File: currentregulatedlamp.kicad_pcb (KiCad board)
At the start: 2 copper layers, 9 parts, among them J1 Conn_01x12, J2 Conn_01x16, U1 TPS54308DDC

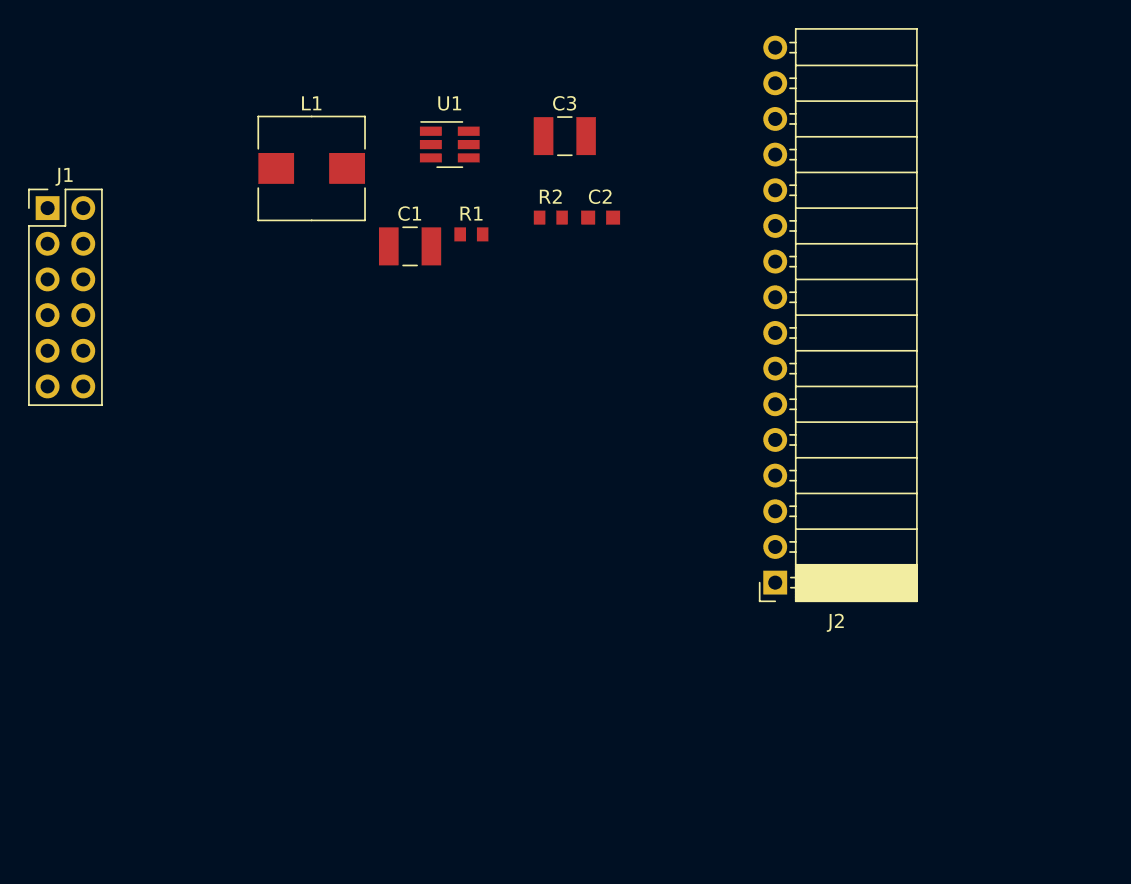
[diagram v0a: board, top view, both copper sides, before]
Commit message: include libraries
added project specific libraries that allow porting the design
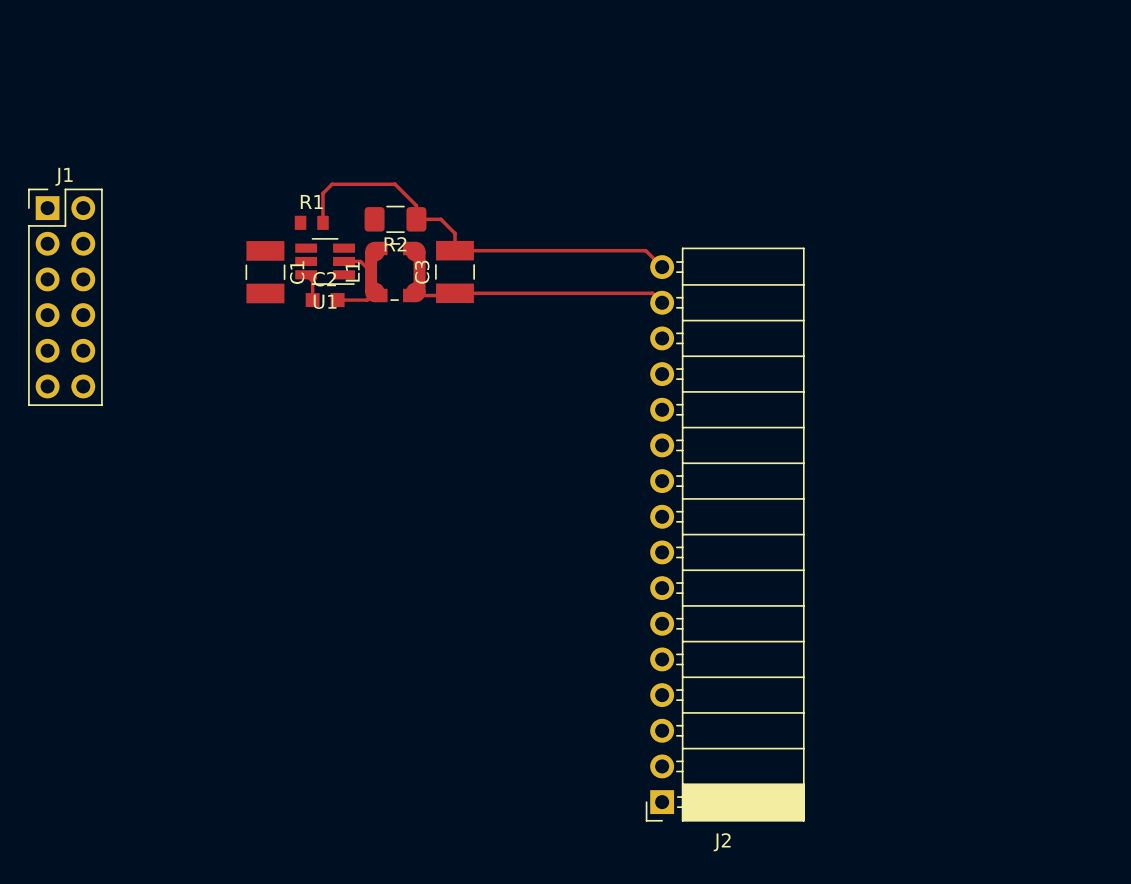
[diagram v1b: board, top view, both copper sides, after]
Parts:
- C2: value C -> 100n/50V
- L1: footprint Inductor_SMD:L_Wuerth_HCM-7070 -> Inductor_SMD:L_Wuerth_WE-TPC-3816
- R2: footprint Resistor_SMD:R_0603_1608Metric -> Resistor_SMD:R_1206_3216Metric_Pad1.42x1.75mm_HandSolder
- moved C2 20.5 mm to (50.8, 51.0)
- moved J2 17.6 mm to (74.8, 86.8)
- moved C3 12.4 mm to (60.0, 49.0), turned to 90 degrees
- moved U1 12.2 mm to (50.8, 48.2), turned to 180 degrees
- moved R1 11.4 mm to (49.8, 45.5)
- moved R2 11.1 mm to (55.8, 45.2), turned to 180 degrees
- moved C1 10.5 mm to (46.5, 49.0), turned to 270 degrees
- moved L1 9.48 mm to (55.8, 49.0), turned to 90 degrees
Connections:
- J2 pad 1: /TPS54200/LED+ -> Net-(J2-Pad1)
- J2 pad 15: Net-(J2-Pad15) -> /TPS54200/LED+
- J2 pad 16: Net-(J2-Pad16) -> /TPS54200/LED-
- J2 pad 2: /TPS54200/LED- -> Net-(J2-Pad2)
- L1 pad 1: /TPS54200/BOOT -> /TPS54200/SW
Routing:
- net /TPS54200/LED-: track 0.00 -> 30.3 mm
- net /TPS54200/LED+: track 0.00 -> 20.4 mm
- net /TPS54200/SW: track 0.00 -> 5.13 mm
- net /TPS54200/BOOT: track 0.00 -> 1.99 mm

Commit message: Schematic replication
decided on path for replicating current regulator
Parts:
- added C1.2: C, Capacitor_SMD:C_1210_3225Metric_Pad1.39x2.70mm_HandSolder, F.Cu at (65.0, 53.5)
- added C2.2: 100n/50V, Capacitor_SMD:C_0603_1608Metric_Pad0.99x1.00mm_HandSolder, F.Cu at (70.2, 56.0)
- added C3.2: C, Capacitor_SMD:C_1210_3225Metric_Pad1.39x2.70mm_HandSolder, F.Cu at (79.5, 54.0)
- added L1.2: L, Inductor_SMD:L_Wuerth_WE-TPC-3816, F.Cu at (75.2, 54.0)
- added R1.2: R, Resistor_SMD:R_0603_1608Metric, F.Cu at (69.3, 50.5)
- added R2.2: R, Resistor_SMD:R_1206_3216Metric_Pad1.42x1.75mm_HandSolder, F.Cu at (75.3, 50.2)
- added U1.2: TPS54308DDC, Package_TO_SOT_SMD:SOT-23-6_Handsoldering, F.Cu at (70.2, 53.2)
- moved J2 21.3 mm to (96.0, 85.7)
- moved J1 3.14 mm to (31.8, 47.5)
- moved C1.1 1.28 mm to (45.2, 48.8)
- renumbered C1 to C1.1, C2 to C2.1, C3 to C3.1, L1 to L1.1, R1 to R1.1, R2 to R2.1, U1 to U1.1
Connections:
- J1 pad 6: Net-(J1-Pad6) -> /LED_2/DIM
- J2 pad 15: /TPS54200/LED+ -> Net-(J2-Pad15)
- J2 pad 16: /TPS54200/LED- -> Net-(J2-Pad16)
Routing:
- net /LED-: track 0.00 -> 50.8 mm
- net /LED+: track 0.00 -> 43.5 mm
- net /TPS54200/LED-: track 30.3 -> 0.00 mm
- net /LED_2/LED-: track 0.00 -> 27.8 mm
- net /TPS54200/LED+: track 20.4 -> 0.00 mm
- net /LED_2/LED+: track 0.00 -> 19.5 mm
- net /LED_2/SW: track 0.00 -> 5.13 mm
- net /LED_2/BOOT: track 0.00 -> 1.99 mm
- net /LED_2/FB: track 0.00 -> 1.97 mm

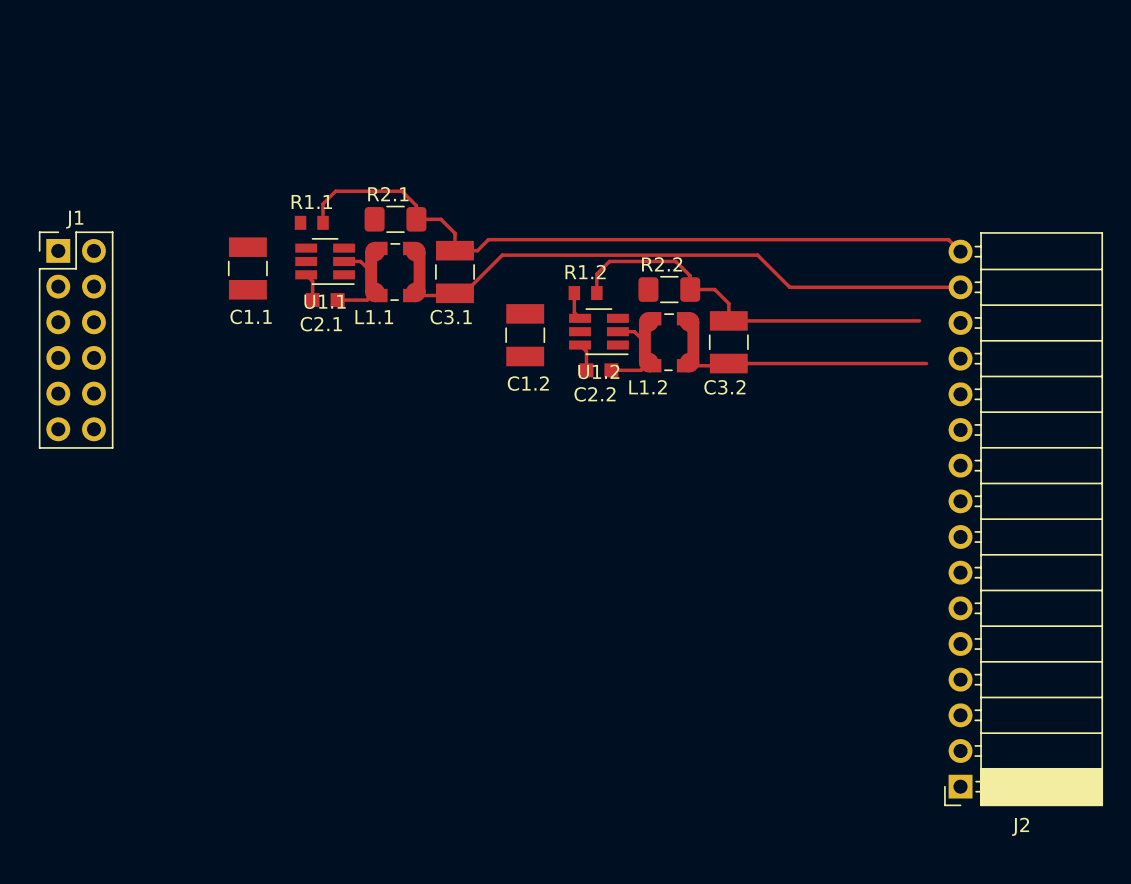
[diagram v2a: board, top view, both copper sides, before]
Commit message: PCB ready for first test run
reduced number of channels to 2 for first prototype
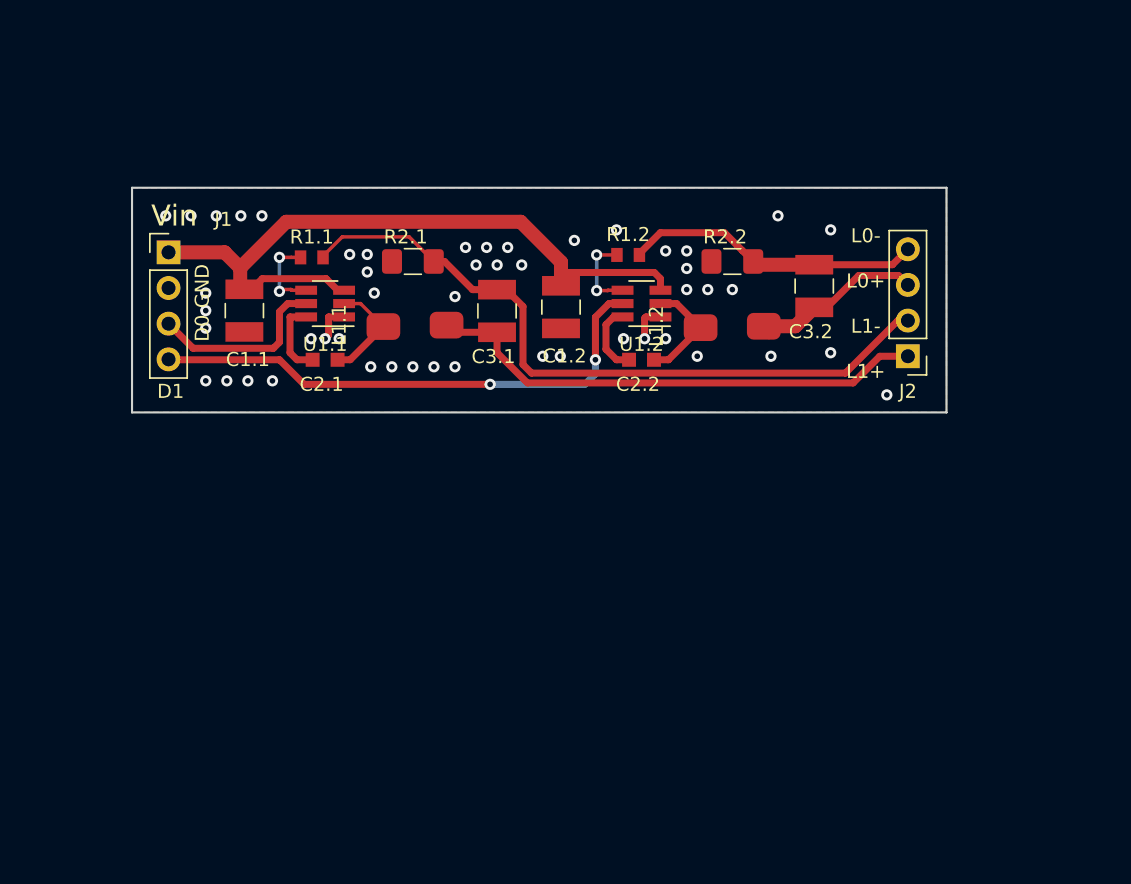
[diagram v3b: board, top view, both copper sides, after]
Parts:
- C1.1, C1.2, C3.1, C3.2: value C -> 10u/25V
- J1: value Conn_01x12 -> Conn_01x04; footprint Connector_PinHeader_2.54mm:PinHeader_2x06_P2.54mm_Vertical -> Connector_PinHeader_2.54mm:PinHeader_1x04_P2.54mm_Vertical
- J2: value Conn_01x16 -> Conn_01x04; footprint Connector_PinSocket_2.54mm:PinSocket_1x16_P2.54mm_Horizontal -> Connector_PinHeader_2.54mm:PinHeader_1x04_P2.54mm_Vertical
- L1.1, L1.2: footprint Inductor_SMD:L_Wuerth_WE-TPC-3816 -> FH_Inductors_SMT:L_Wuerth_WE-PD-6050
- R1.1, R1.2: value R -> 1k/5%
- U1.1, U1.2: value TPS54308DDC -> TPS54200DDC
- moved J2 30.9 mm to (92.2, 55.0)
- moved J1 7.85 mm to (39.6, 47.6)
- moved C3.2 7.28 mm to (85.6, 50.0)
- moved R2.2 4.91 mm to (79.8, 48.2)
- moved L1.2 4.63 mm to (79.7, 52.9), turned to 270 degrees
- moved C2.1 4.25 mm to (50.8, 55.2)
- moved C3.1 4.08 mm to (63.0, 51.8)
- moved R1.2 4.07 mm to (72.3, 47.8)
- moved L1.1 4.03 mm to (57.1, 52.8), turned to 270 degrees
- moved U1.2 3.63 mm to (73.3, 51.2)
- moved R2.1 3.25 mm to (57.0, 48.2)
- moved C1.2 3.24 mm to (67.5, 51.5)
- moved C2.2 3.12 mm to (73.3, 55.2)
- moved C1.1 3.01 mm to (45.0, 51.8)
- moved U1.1 3.00 mm to (50.8, 51.2)
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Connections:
- C3.1 pad 1: /TPS54200/LED+ -> /LED+
- C3.1 pad 2: /TPS54200/LED- -> /LED-
- C3.2 pad 1: /LED_2/LED+ -> /LED+_1
- C3.2 pad 2: /LED_2/LED- -> /LED-_1
- J1 pad 2: +24V -> GND
- J1 pad 3: GND -> /DIM
- J1 pad 4: GND -> /DIM_1
- J2 pad 1: Net-(J2-Pad1) -> /LED+
- J2 pad 2: Net-(J2-Pad2) -> /LED-
- J2 pad 3: Net-(J2-Pad3) -> /LED+_1
- J2 pad 4: Net-(J2-Pad4) -> /LED-_1
- L1.1 pad 2: /TPS54200/LED+ -> /LED+
- L1.2 pad 2: /LED_2/LED+ -> /LED+_1
- R1.1 pad 2: /TPS54200/LED- -> /LED-
- R1.2 pad 2: /LED_2/LED- -> /LED-_1
- R2.1 pad 1: /TPS54200/LED- -> /LED-
- R2.2 pad 1: /LED_2/LED- -> /LED-_1
- U1.1 pad 5: /TPS54200/DIM -> /DIM
- U1.2 pad 5: /LED_2/DIM -> /DIM_1
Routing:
- net +24V: track 0.00 -> 51.6 mm
- net /DIM_1: track 0.00 -> 43.5 mm, vias 0 -> 2
- net /LED_2/LED-: track 27.8 -> 0.00 mm
- net /LED-_1: track 0.00 -> 21.8 mm, vias 0 -> 1
- net /LED_2/LED+: track 19.5 -> 0.00 mm
- net /DIM: track 0.00 -> 13.1 mm
- net /LED+_1: track 0.00 -> 12.3 mm
- net /LED+: track 43.5 -> 36.8 mm
- net /TPS54200/FB: track 0.00 -> 5.98 mm, vias 0 -> 2
- net GND: track 0.00 -> 5.38 mm, vias 0 -> 50
- net /LED_2/FB: track 1.97 -> 5.84 mm, vias 0 -> 2
- net /TPS54200/BOOT: track 1.99 -> 5.52 mm
- net /LED_2/BOOT: track 1.99 -> 5.11 mm
- net /LED_2/SW: track 5.13 -> 7.84 mm
- net /TPS54200/SW: track 5.13 -> 7.26 mm
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- added copper zone on B.Cu, net GND
- added copper zone on F.Cu, net GND
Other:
- board outline added: 58 x 16 mm
- board text added: "D0"
- board text added: "D1"
- board text added: "GND"
- board text added: "L0- L0+ L1- L1+"
- board text added: "Vin"

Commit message: silkscreen bottom layer
added KiCAD and OSHW logo to bottom
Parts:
- added REF**: OSHW-Logo2_7.3x6mm_SilkScreen, Symbol:OSHW-Logo2_7.3x6mm_SilkScreen, B.Cu at (71.5, 51.5)
- added REF**: KiCad-Logo_5mm_SilkScreen, Symbol:KiCad-Logo_5mm_SilkScreen, B.Cu at (82.0, 52.8)
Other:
- board text added: "current regulator for output currents 0.35A-1A based on TPS54201 2019/05 ver1.0"
- board text added: "https://github.com/FHdB/"
